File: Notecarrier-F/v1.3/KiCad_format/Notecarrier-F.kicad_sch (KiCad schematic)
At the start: 17 parts

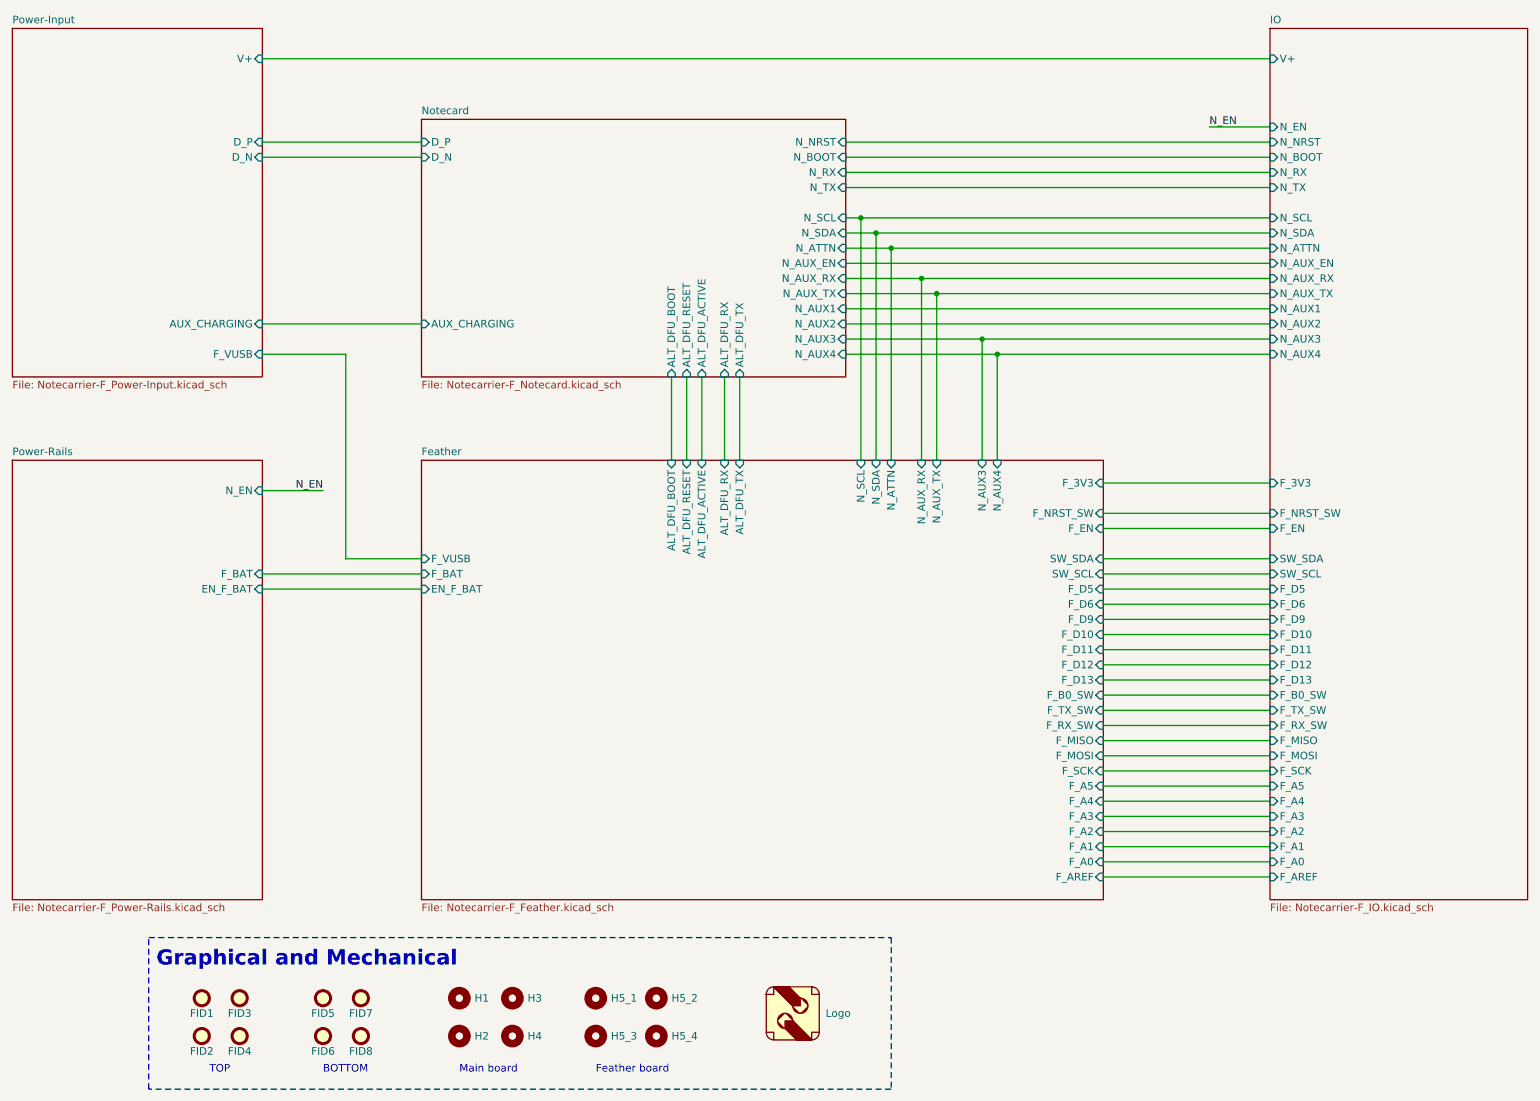
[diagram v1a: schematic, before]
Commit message: Notecarrier-F v1.3: KiCad 9 port from the release-day Altium sources
Replace the hand-made KiCad 7 port (which described v1.2, with a half-applied
v1.3 schematic delta and an ERRATA file) with a direct import of the v1.3
Altium project, recovered from the design archive's history: committed by the
design house on 2023-07-10, the day of the 2200-814 fabrication package, with a
Rev 11 schematic PDF byte-identical to the one published here. The Altium
sources are published alongside as Notecarrier-F/v1.3/Altium, as for v1.5.

The port follows the v1.5 procedure (KiCad 9.0.9 Altium project importer plus
scripted cleanup, scripts kept under documentation/scripts). All validation
gates pass: ERC 0, DRC 0 with schematic parity, BOM exact (94/94 vs
3000-653-002), placement 89/89 vs PNP-3000-653-002, gerber diff exact on outer
copper and masks with the reviewed inner-annulus/silk classes frozen as the
baseline, KiCanvas and RAG. The KiCad netlist was also matched pad by pad
against the nets carried by the Altium board file (0 conflicts).

J9/J10 are fitted per the released BOM (the 2023-08-31 re-save of the project
flips the variant to match); J11/R11/R12 are DNP. Design rules follow the
board's own Altium rule set (0.1 mm clearance). The old hand-port notes are
kept as History_Porting-Notes-hand-port.md because the harness README cites
them for the gerber-diff recipe; the RAG exclusion comment and the product
README are updated accordingly.

Co-Authored-By: Claude Fable 5.1 <noreply@anthropic.com>
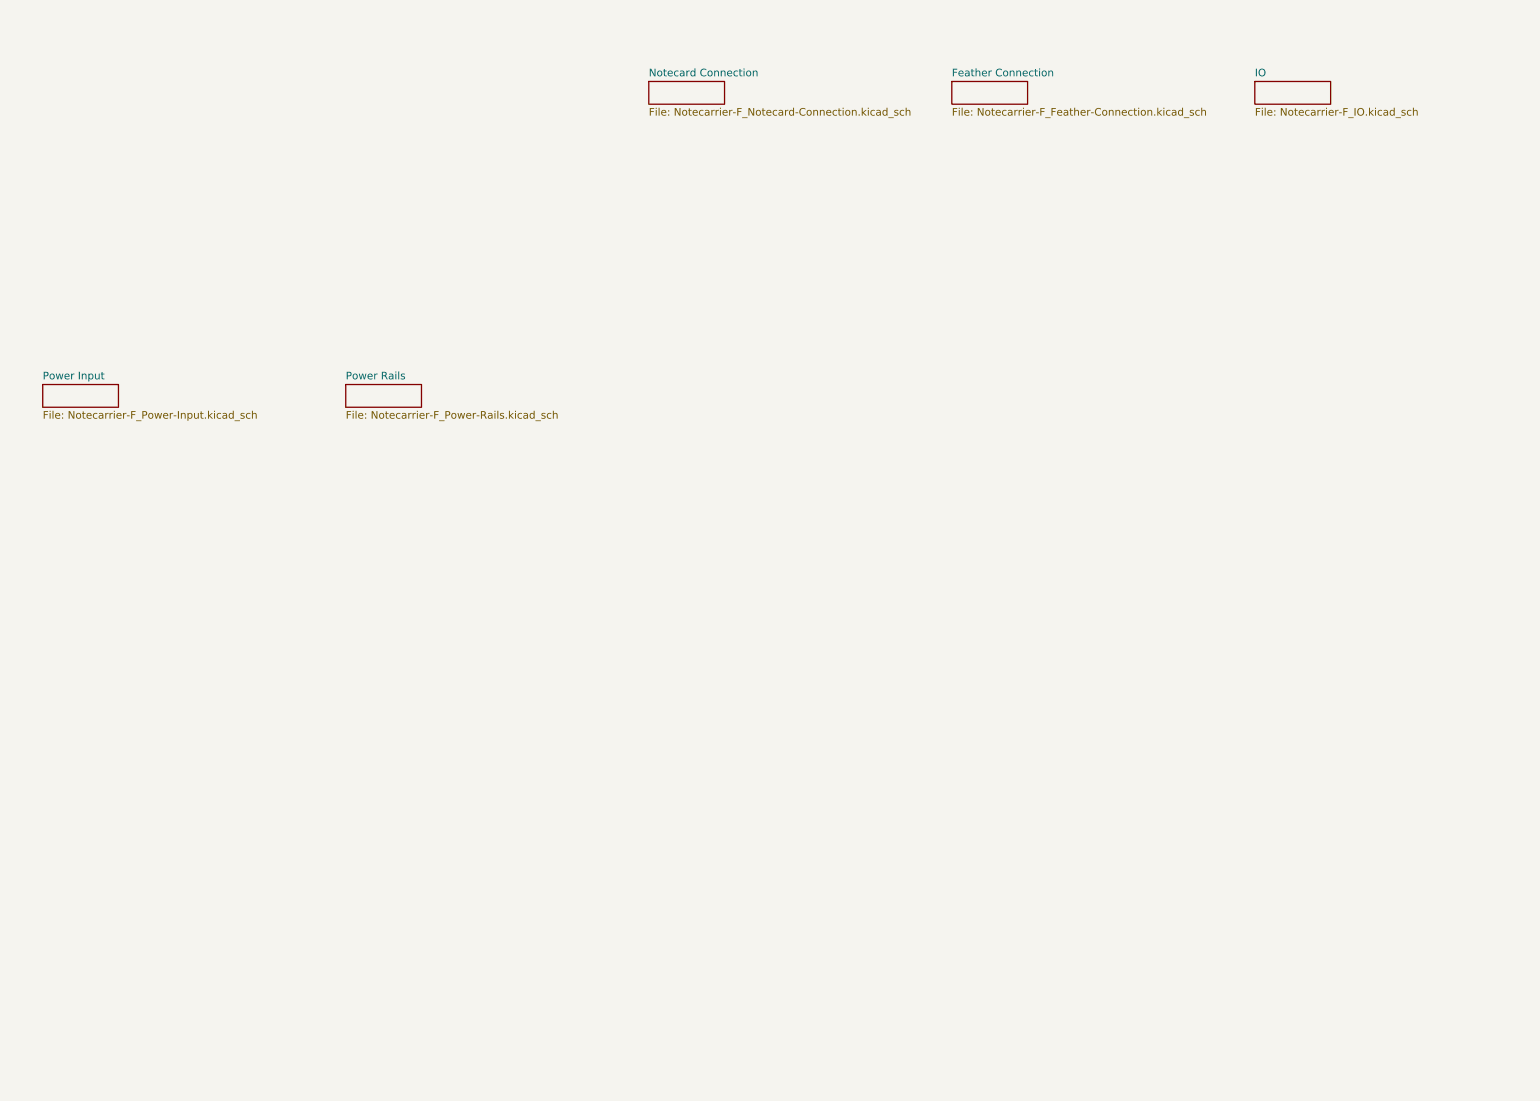
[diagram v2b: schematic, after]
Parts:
- removed FID1, FID2, FID3, FID4, FID5, FID6, FID7, FID8: TPS, blues-kicad-lib:Fiducial mark 1mm_Fv1.2, symbol Mechanical:Fiducial
- removed G1: Logo, blues-kicad-lib:Logo_23.5x6.1, symbol blues-kicad-lib:Logo_Blues_Wireless
- removed H1, H2, H3, H4: MountingHole, blues-kicad-lib:MountingHole_3.3mm_no-courtyard, symbol Mechanical:MountingHole
- removed H5_1, H5_2, H5_3, H5_4: MountingHole, blues-kicad-lib:MountingHole_2.54mm_no-courtyard, symbol Mechanical:MountingHole
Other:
- removed sheet Feather
- removed sheet Notecard
- removed sheet Power-Input
- removed sheet Power-Rails
- added sheet Feather Connection (Notecarrier-F_Feather-Connection.kicad_sch)
- added sheet Notecard Connection (Notecarrier-F_Notecard-Connection.kicad_sch)
- added sheet Power Input (Notecarrier-F_Power-Input.kicad_sch)
- added sheet Power Rails (Notecarrier-F_Power-Rails.kicad_sch)
- sheet IO ports: added none; removed F_3V3, F_A0, F_A1, F_A2, F_A3, F_A4, F_A5, F_AREF, F_B0_SW, F_D10, F_D11, F_D12, F_D13, F_D5, F_D6, F_D9, F_EN, F_MISO, F_MOSI, F_NRST_SW, F_RX_SW, F_SCK, F_TX_SW, N_ATTN, N_AUX1, N_AUX2, N_AUX3, N_AUX4, N_AUX_EN, N_AUX_RX, N_AUX_TX, N_BOOT, N_EN, N_NRST, N_RX, N_SCL, N_SDA, N_TX, SW_SCL, SW_SDA, V+
- note removed: "BOTTOM"
- note removed: "Feather board"
- note removed: "Graphical and Mechanical"
- note removed: "Main board"
- note removed: "TOP"
- company: (none) -> Byte Lab Grupa d.o.o.
